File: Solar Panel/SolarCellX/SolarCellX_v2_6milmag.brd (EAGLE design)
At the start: 100 x 82 mm, 16 parts

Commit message: Fixed??? Solar Panel X Final + MB
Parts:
- moved 2 2.54 mm to (55.4, 32.5)
- moved 11 0.63 mm to (94.0, 15.5)
- moved 1 0.51 mm to (50.3, 67.0)
- moved 23 0.27 mm to (6.08, 67.0)
- moved 13 0.09 mm to (49.7, 15.5)
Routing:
- net GND: track 96.3 -> 88.6 mm
- net V_SOLAR: track 107.2 -> 112.6 mm
- net N$4: track 107.2 -> 110.4 mm
- net N$1: track 54699.3 -> 54698.4 mm
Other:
- board text added: "PandaSat Solar Cell X Board Rev A"

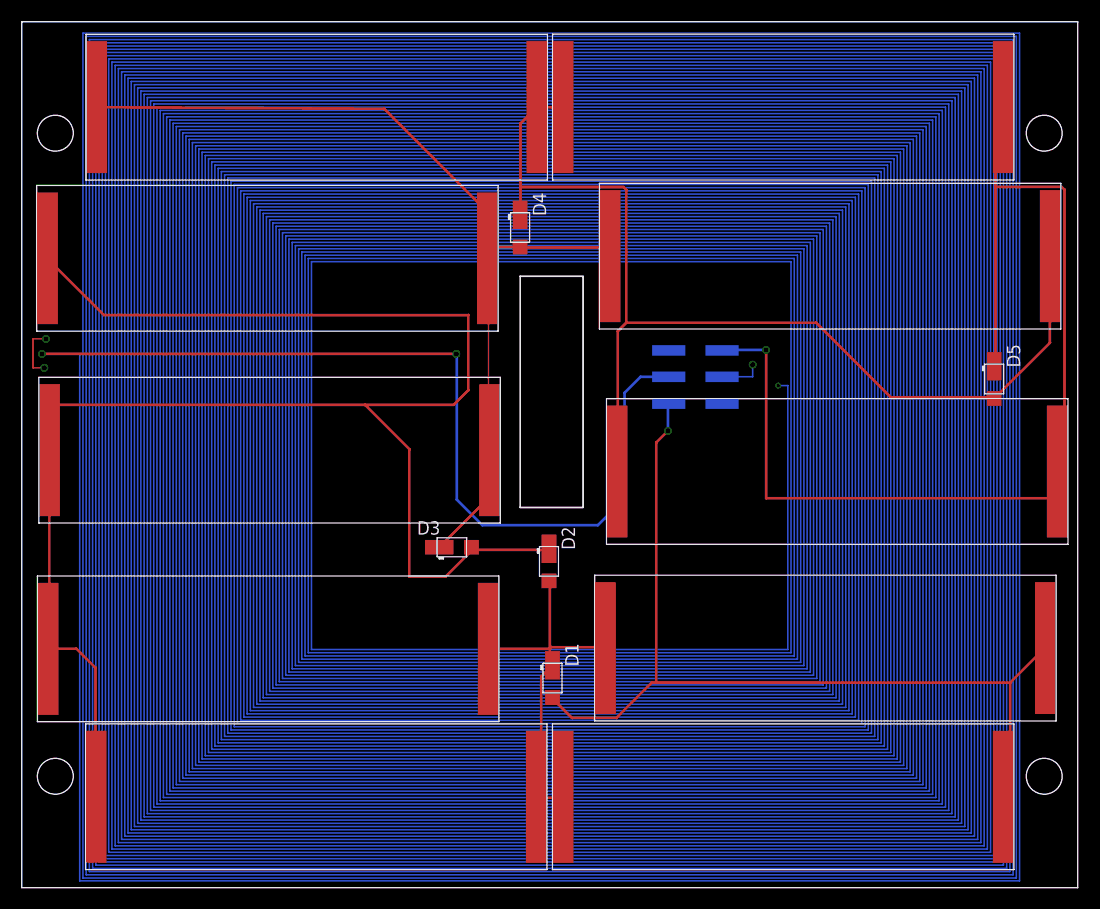
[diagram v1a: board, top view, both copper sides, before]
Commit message: Solar Panel Gerbers Final X, DRC updates for MB
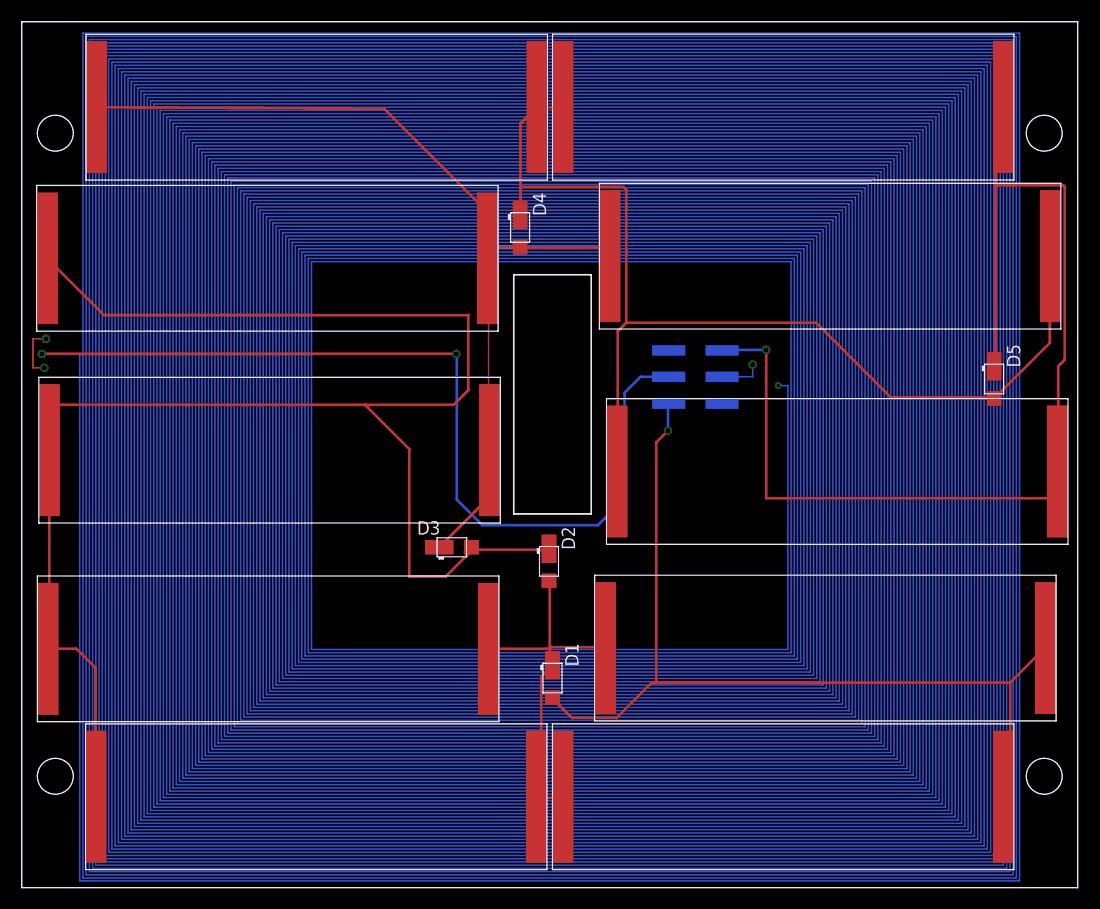
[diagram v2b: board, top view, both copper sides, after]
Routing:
- net N$1: track 54698.4 -> 54675.6 mm
- net V_SOLAR: track 112.6 -> 111.3 mm
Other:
- outline, holes or cut-outs redrawn
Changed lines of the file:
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@@
 <layer number="18" name="Vias" color="2" fill="1" visible="yes" active="yes"/>
 <layer number="19" name="Unrouted" color="6" fill="1" visible="yes" active="yes"/>
-<layer number="20" name="Dimension" color="24" fill="1" visible="no" active="yes"/>
+<layer number="20" name="Dimension" color="24" fill="1" visible="yes" active="yes"/>
 <layer number="21" name="tPlace" color="7" fill="1" visible="no" active="yes"/>
 <layer number="22" name="bPlace" color="7" fill="1" visible="yes" active="yes"/>
@@
 <layer number="44" name="Drills" color="7" fill="1" visible="no" active="yes"/>
 <layer number="45" name="Holes" color="7" fill="1" visible="yes" active="yes"/>
-<layer number="46" name="Milling" color="3" fill="1" visible="no" active="yes"/>
+<layer number="46" name="Milling" color="3" fill="1" visible="yes" active="yes"/>
 <layer number="47" name="Measures" color="7" fill="1" visible="no" active="yes"/>
 <layer number="48" name="Document" color="7" fill="1" visible="no" active="yes"/>
@@
 <wire x1="100" y1="82" x2="100" y2="0" width="0.127" layer="20"/>
 <wire x1="100" y1="0" x2="0" y2="0" width="0.127" layer="20"/>
-<wire x1="47.1946" y1="57.895578125" x2="53.1562375" y2="57.895578125" width="0.1524" layer="20"/>
-<wire x1="53.1562375" y1="57.895578125" x2="53.1562375" y2="36.006859375" width="0.1524" layer="20"/>
-<wire x1="53.1562375" y1="36.006859375" x2="47.1946" y2="36.006859375" width="0.1524" layer="20"/>
-<wire x1="47.1946" y1="36.006859375" x2="47.1946" y2="57.895578125" width="0.1524" layer="20"/>
+<wire x1="46.585" y1="58.047978125" x2="53.9182375" y2="58.047978125" width="0.1524" layer="46"/>
+<wire x1="53.9182375" y1="58.047978125" x2="53.9182375" y2="35.397259375" width="0.1524" layer="46"/>
+<wire x1="53.9182375" y1="35.397259375" x2="46.585" y2="35.397259375" width="0.1524" layer="46"/>
+<wire x1="46.585" y1="35.397259375" x2="46.585" y2="58.047978125" width="0.1524" layer="46"/>
 <text x="35.9664" y="42.8244" size="1.778" layer="22" rot="MR270" align="center">PandaSat
 Solar Cell X Board
@@
 <param name="rlMinPadBottom" value="4mil"/>
 <param name="rlMaxPadBottom" value="20mil"/>
-<param name="rlMinViaOuter" value="4mil"/>
+<param name="rlMinViaOuter" value="6mil"/>
 <param name="rlMaxViaOuter" value="20mil"/>
-<param name="rlMinViaInner" value="4mil"/>
+<param name="rlMinViaInner" value="6mil"/>
 <param name="rlMaxViaInner" value="20mil"/>
 <param name="rlMinMicroViaOuter" value="4mil"/>
@@
 <contactref element="D5" pad="NEG"/>
 <contactref element="U$1" pad="P$6"/>
-<wire x1="92.202" y1="72.644" x2="92.202" y2="66.3575" width="0.254" layer="1"/>
-<wire x1="92.202" y1="66.3575" x2="92.202" y2="49.4538" width="0.254" layer="1"/>
+<wire x1="92.202" y1="72.644" x2="92.202" y2="66.5099" width="0.254" layer="1"/>
+<wire x1="92.202" y1="66.5099" x2="92.202" y2="49.4538" width="0.254" layer="1"/>
 <wire x1="93.4593" y1="73.9013" x2="92.202" y2="72.644" width="0.254" layer="1"/>
 <wire x1="92.202" y1="49.4538" x2="92.083" y2="49.371" width="0.1524" layer="1"/>
@@
 <wire x1="98.0694" y1="36.8808" x2="70.485" y2="36.8808" width="0.254" layer="1"/>
 <wire x1="98.0694" y1="36.8808" x2="98.072" y2="39.412" width="0.1524" layer="1"/>
-<wire x1="98.4885" y1="66.3575" x2="92.202" y2="66.3575" width="0.254" layer="1"/>
-<wire x1="98.7552" y1="66.0908" x2="98.4885" y2="66.3575" width="0.254" layer="1"/>
-<wire x1="98.7552" y1="37.4269" x2="98.7552" y2="66.0908" width="0.254" layer="1"/>
+<wire x1="98.6409" y1="66.5099" x2="92.202" y2="66.5099" width="0.254" layer="1"/>
+<wire x1="98.7552" y1="66.3956" x2="98.6409" y2="66.5099" width="0.254" layer="1"/>
 <wire x1="98.2091" y1="36.8808" x2="98.7552" y2="37.4269" width="0.1524" layer="1"/>
-<wire x1="98.2091" y1="36.8808" x2="98.072" y2="39.412" width="0.1524" layer="1"/>
+<wire x1="98.2091" y1="36.8808" x2="98.077228125" y2="39.315496875" width="0.1524" layer="1"/>
+<wire x1="98.077228125" y1="39.315496875" x2="98.072" y2="39.412" width="0.1524" layer="1"/>
 <wire x1="70.485" y1="36.8808" x2="70.485" y2="50.927" width="0.254" layer="1"/>
 <wire x1="66.315" y1="50.879" x2="66.315" y2="50.927" width="0.1524" layer="16"/>
 <wire x1="66.315" y1="50.927" x2="70.485" y2="50.927" width="0.254" layer="16"/>
 <via x="70.485" y="50.927" extent="1-16" drill="0.5"/>
+<wire x1="98.7552" y1="66.3956" x2="98.7552" y2="49.9872" width="0.254" layer="1"/>
+<wire x1="98.7552" y1="49.9872" x2="98.1456" y2="49.3776" width="0.254" layer="1"/>
+<wire x1="98.1456" y1="49.3776" x2="98.1456" y2="39.38386875" width="0.254" layer="1"/>
+<wire x1="98.1456" y1="39.38386875" x2="98.077228125" y2="39.315496875" width="0.254" layer="1"/>
 </signal>
 <signal name="N$1">
@@
 <contactref element="U$1" pad="P$4"/>
 <contactref element="U$1" pad="P$3"/>
-<wire x1="61.265" y1="48.379" x2="60.487759375" y2="48.379" width="0.254" layer="16"/>
 <wire x1="41.148" y1="50.546" x2="41.195115625" y2="50.546" width="0.254" layer="16"/>
 <via x="41.148" y="50.546" extent="1-16" drill="0.5"/>
@@
 <wire x1="27.432" y1="22.5552" x2="72.5424" y2="22.5552" width="0.1524" layer="2"/>
 <wire x1="5.4864" y1="0.6477" x2="5.4864" y2="51.9684" width="0.1524" layer="2"/>
-<wire x1="72.5424" y1="53.0264" x2="58.2168" y2="53.0264" width="0.1524" layer="2"/>
+<wire x1="72.5424" y1="53.0264" x2="71.628" y2="53.0264" width="0.1524" layer="2"/>
 <wire x1="72.5424" y1="22.5552" x2="72.5424" y2="53.0264" width="0.1524" layer="2"/>
 <wire x1="27.7368" y1="58.9788" x2="72.5424" y2="58.9788" width="0.1524" layer="15"/>
@@
 <wire x1="5.7912" y1="80.9244" x2="5.7912" y2="49.2252" width="0.1524" layer="15"/>
 <wire x1="5.7912" y1="49.2252" x2="2.1336" y2="49.2252" width="0.1524" layer="15"/>
-<wire x1="58.2168" y1="53.0264" x2="58.2168" y2="49.53" width="0.1524" layer="2"/>
+<wire x1="71.628" y1="53.0264" x2="71.628" y2="50.8762" width="0.1524" layer="2"/>
+<wire x1="71.628" y1="50.8762" x2="70.2818" y2="49.53" width="0.1524" layer="2"/>
+<wire x1="69.215" y1="49.53" x2="70.2818" y2="49.53" width="0.1524" layer="2"/>
 <wire x1="72.5424" y1="58.9788" x2="72.5424" y2="47.5167" width="0.1524" layer="15"/>
 <wire x1="5.4864" y1="51.9684" x2="2.286" y2="51.9684" width="0.1524" layer="2"/>
 <via x="2.286" y="51.9684" extent="1-16" drill="0.5"/>
-<wire x1="58.2168" y1="49.53" x2="69.215" y2="49.53" width="0.1524" layer="2"/>
 <wire x1="66.315" y1="48.379" x2="66.315" y2="48.387" width="0.1524" layer="16"/>
 <wire x1="66.315" y1="48.387" x2="69.215" y2="48.387" width="0.1524" layer="16"/>
@@
 <wire x1="54.556478125" y1="34.327915625" x2="57.0830875" y2="36.854525" width="0.254" layer="16"/>
 <wire x1="57.0830875" y1="36.854525" x2="57.0830875" y2="46.86466875" width="0.254" layer="16"/>
-<wire x1="58.59741875" y1="48.379" x2="60.487759375" y2="48.379" width="0.254" layer="16"/>
+<wire x1="58.59741875" y1="48.379" x2="61.265" y2="48.379" width="0.254" layer="16"/>
 <wire x1="57.0830875" y1="46.86466875" x2="58.59741875" y2="48.379" width="0.254" layer="16"/>
 <wire x1="27.432" y1="22.5552" x2="72.5424" y2="22.5552" width="0.1524" layer="16"/>

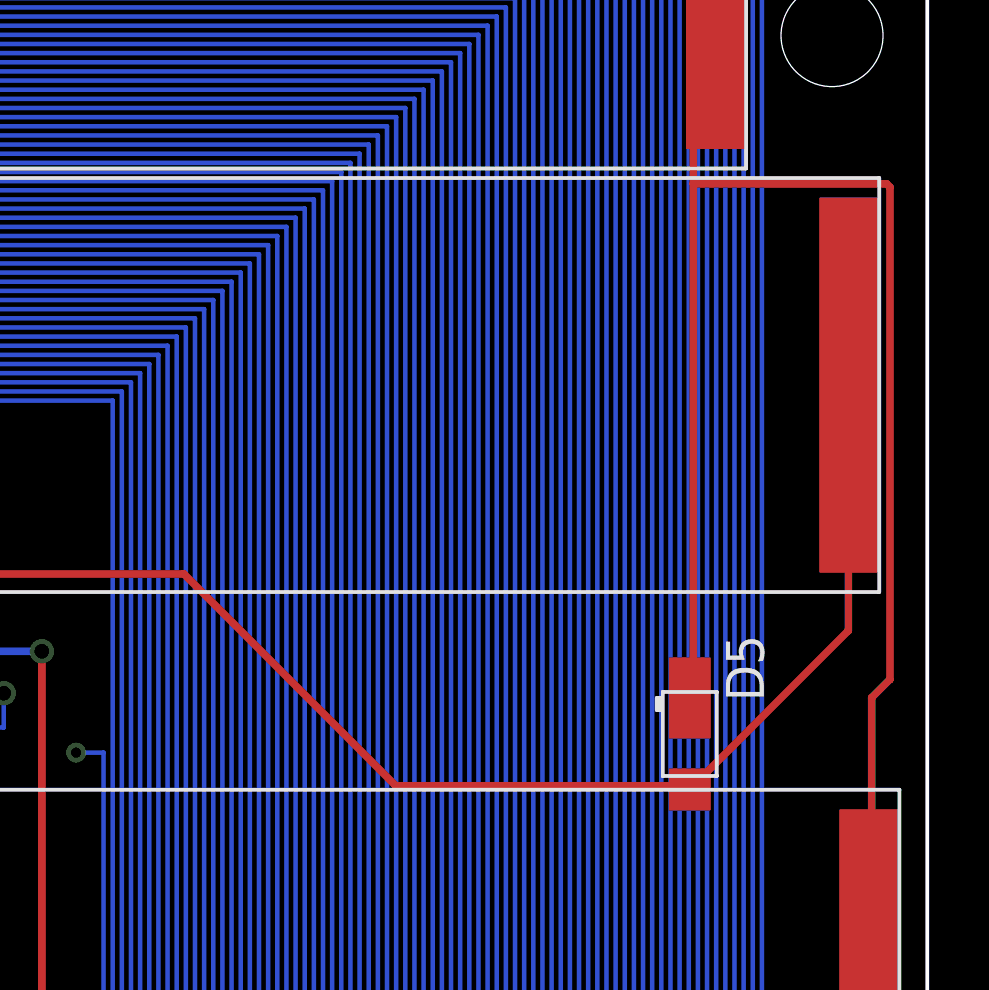
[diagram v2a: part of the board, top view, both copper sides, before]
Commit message: Resolved a diode issue on SolarCellX and pushed new gerber
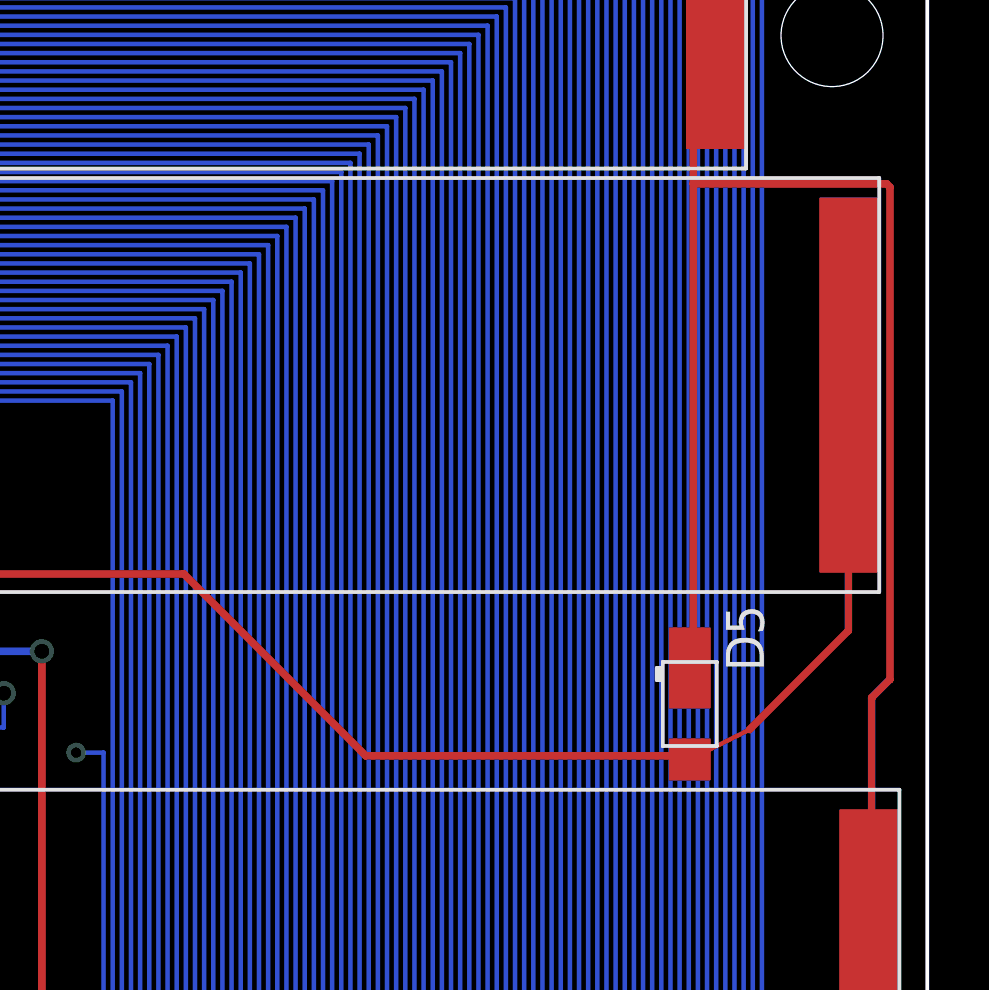
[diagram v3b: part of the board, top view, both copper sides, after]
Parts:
- moved D5 1.00 mm to (92.1, 49.2)
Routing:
- net N$4: track 110.4 -> 109.4 mm
- net V_SOLAR: track 111.3 -> 110.3 mm
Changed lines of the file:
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@@
 <?xml version="1.0" encoding="utf-8"?>
 <!DOCTYPE eagle SYSTEM "eagle.dtd">
-<eagle version="9.2.2">
+<eagle version="9.3.0">
 <drawing>
 <settings>
@@
 <setting verticaltext="up"/>
 </settings>
-<grid distance="6" unitdist="mil" unit="mil" style="lines" multiple="1" display="yes" altdistance="1" altunitdist="mm" altunit="mm"/>
+<grid distance="1" unitdist="mm" unit="mm" style="lines" multiple="1" display="yes" altdistance="1" altunitdist="mm" altunit="mm"/>
 <layers>
 <layer number="1" name="Top" color="4" fill="1" visible="yes" active="yes"/>
-<layer number="2" name="Route2" color="16" fill="1" visible="yes" active="yes"/>
+<layer number="2" name="Route2" color="16" fill="1" visible="no" active="yes"/>
 <layer number="3" name="Route3" color="17" fill="1" visible="no" active="no"/>
 <layer number="4" name="Route4" color="18" fill="1" visible="no" active="no"/>
@@
 <layer number="13" name="Route13" color="21" fill="1" visible="no" active="no"/>
 <layer number="14" name="Route14" color="22" fill="1" visible="no" active="no"/>
-<layer number="15" name="Route15" color="23" fill="1" visible="yes" active="yes"/>
-<layer number="16" name="Bottom" color="1" fill="1" visible="yes" active="yes"/>
+<layer number="15" name="Route15" color="23" fill="1" visible="no" active="yes"/>
+<layer number="16" name="Bottom" color="1" fill="1" visible="no" active="yes"/>
 <layer number="17" name="Pads" color="2" fill="1" visible="yes" active="yes"/>
 <layer number="18" name="Vias" color="2" fill="1" visible="yes" active="yes"/>
 <layer number="19" name="Unrouted" color="6" fill="1" visible="yes" active="yes"/>
 <layer number="20" name="Dimension" color="24" fill="1" visible="yes" active="yes"/>
-<layer number="21" name="tPlace" color="7" fill="1" visible="no" active="yes"/>
+<layer number="21" name="tPlace" color="7" fill="1" visible="yes" active="yes"/>
 <layer number="22" name="bPlace" color="7" fill="1" visible="yes" active="yes"/>
-<layer number="23" name="tOrigins" color="15" fill="1" visible="no" active="yes"/>
-<layer number="24" name="bOrigins" color="15" fill="1" visible="no" active="yes"/>
+<layer number="23" name="tOrigins" color="15" fill="1" visible="yes" active="yes"/>
+<layer number="24" name="bOrigins" color="15" fill="1" visible="yes" active="yes"/>
 <layer number="25" name="tNames" color="7" fill="1" visible="no" active="yes"/>
 <layer number="26" name="bNames" color="7" fill="1" visible="no" active="yes"/>
@@
 <attribute name="NAME" x="48.39" y="65.822" size="1.27" layer="25" rot="R270"/>
 </element>
-<element name="D5" library="Solar" package="SB_DIODE" value="SB_DIODE" x="92.083" y="48.171" smashed="yes" rot="R270">
-<attribute name="NAME" x="93.283" y="51.471" size="1.27" layer="25" rot="R270"/>
+<element name="D5" library="Solar" package="SB_DIODE" value="SB_DIODE" x="92.083" y="49.171" smashed="yes" rot="R270">
+<attribute name="NAME" x="93.283" y="52.471" size="1.27" layer="25" rot="R270"/>
 </element>
 <element name="11" library="Solar" package="SLMD121H04L" value="SLMD121H04L" x="93.9546" y="15.51" smashed="yes" rot="R180"/>
@@
 <contactref element="1" pad="P$1"/>
 <contactref element="2" pad="P$1"/>
-<wire x1="92.202" y1="46.4439" x2="92.202" y2="46.3804" width="0.1524" layer="1"/>
-<wire x1="97.3709" y1="51.6128" x2="92.202" y2="46.4439" width="0.254" layer="1"/>
+<wire x1="97.3709" y1="51.6128" x2="94.07185625" y2="48.31375625" width="0.254" layer="1"/>
 <wire x1="97.3709" y1="59.7916" x2="97.3709" y2="51.6128" width="0.254" layer="1"/>
-<wire x1="92.202" y1="46.3804" x2="92.083" y2="46.321" width="0.1524" layer="1"/>
+<wire x1="94.07185625" y1="48.31375625" x2="92.083" y2="47.321" width="0.1524" layer="1"/>
 <wire x1="97.3709" y1="59.7916" x2="97.399" y2="59.803" width="0.1524" layer="1"/>
 <wire x1="47.2186" y1="72.3646" x2="47.2186" y2="66.3575" width="0.254" layer="1"/>
@@
 <wire x1="51.689" y1="73.9013" x2="51.26" y2="73.92" width="0.1524" layer="1"/>
 <wire x1="48.6156" y1="73.7616" x2="48.7796" y2="73.9114" width="0.1524" layer="1"/>
-<wire x1="82.279" y1="46.4439" x2="92.202" y2="46.4439" width="0.254" layer="1"/>
-<wire x1="75.2178" y1="53.5051" x2="82.279" y2="46.4439" width="0.254" layer="1"/>
+<wire x1="81.279" y1="47.4439" x2="92.202" y2="47.4439" width="0.254" layer="1"/>
+<wire x1="75.2178" y1="53.5051" x2="81.279" y2="47.4439" width="0.254" layer="1"/>
 <wire x1="57.2516" y1="53.5051" x2="75.2178" y2="53.5051" width="0.254" layer="1"/>
 </signal>
@@
 <contactref element="U$1" pad="P$6"/>
 <wire x1="92.202" y1="72.644" x2="92.202" y2="66.5099" width="0.254" layer="1"/>
-<wire x1="92.202" y1="66.5099" x2="92.202" y2="49.4538" width="0.254" layer="1"/>
+<wire x1="92.202" y1="66.5099" x2="92.202" y2="50.4538" width="0.254" layer="1"/>
 <wire x1="93.4593" y1="73.9013" x2="92.202" y2="72.644" width="0.254" layer="1"/>
-<wire x1="92.202" y1="49.4538" x2="92.083" y2="49.371" width="0.1524" layer="1"/>
+<wire x1="92.202" y1="50.4538" x2="92.083" y2="50.371" width="0.1524" layer="1"/>
 <wire x1="93.4593" y1="73.9013" x2="92.96" y2="73.92" width="0.1524" layer="1"/>
 <wire x1="98.0694" y1="36.8808" x2="70.485" y2="36.8808" width="0.254" layer="1"/>
